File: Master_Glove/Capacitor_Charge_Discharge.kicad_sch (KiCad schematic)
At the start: 22 parts, among them Q1 NPN, Q2 PNP, Q3 NPN, SW1 SW_Push, U2 OPA2340, U3 MIC1553YM5-TR, U4 TC7WH02FU, U5 NC7SZ57P6X, U6 74AHC1G14, U7 TC7WH02FU

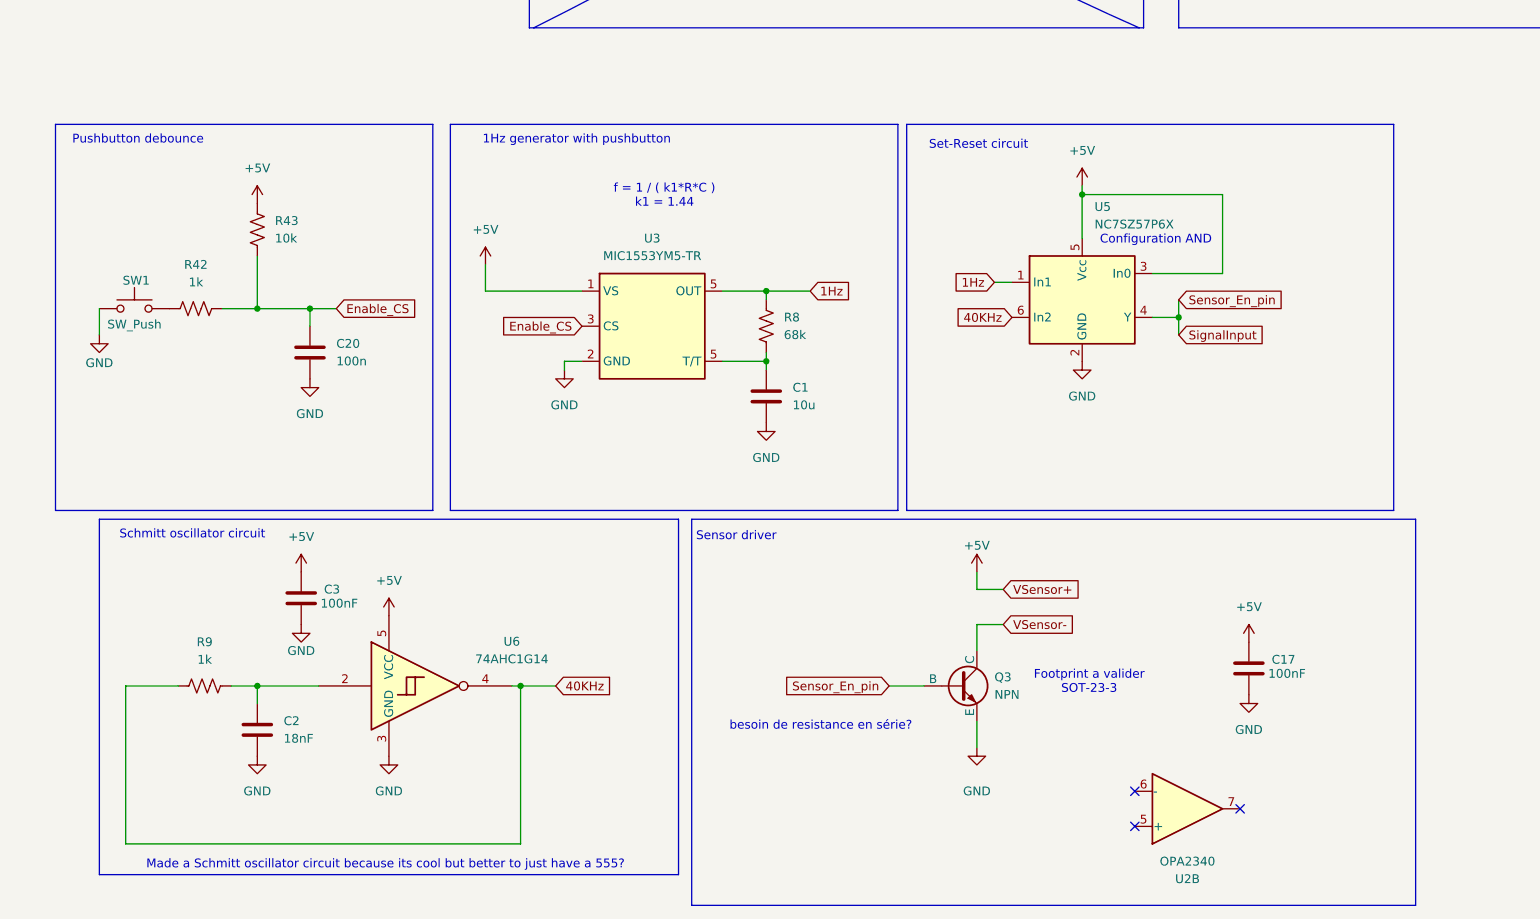
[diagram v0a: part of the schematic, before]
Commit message: fix bug
added comment for resistor in series for sensor not needed since already built in NPN
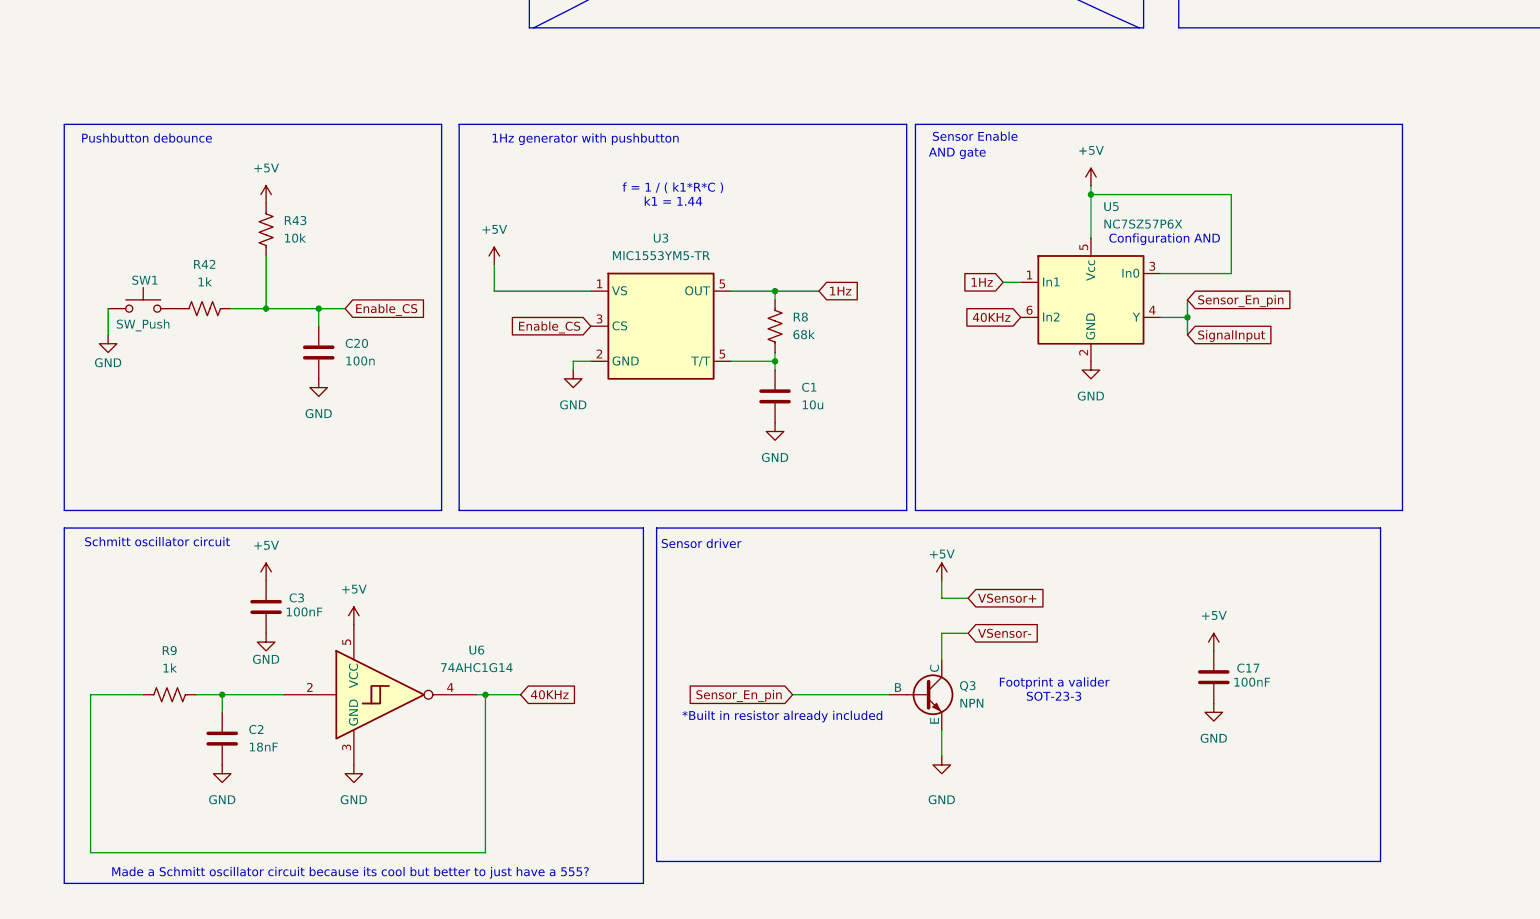
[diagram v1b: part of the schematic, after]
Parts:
- removed U2: OPA2340, symbol Amplifier_Operational:OPA2340
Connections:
- no-connect marks 6 -> 3
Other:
- note added: "*Built in resistor already included"
- note added: "AND gate"
- note added: "Sensor Enable"
- note removed: "Set-Reset circuit"
- note removed: "besoin de resistance en série?"
- moved on the sheet: C1, C17, C2, C20, C3, Q3, R42, R43, R8, R9, SW1, U3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

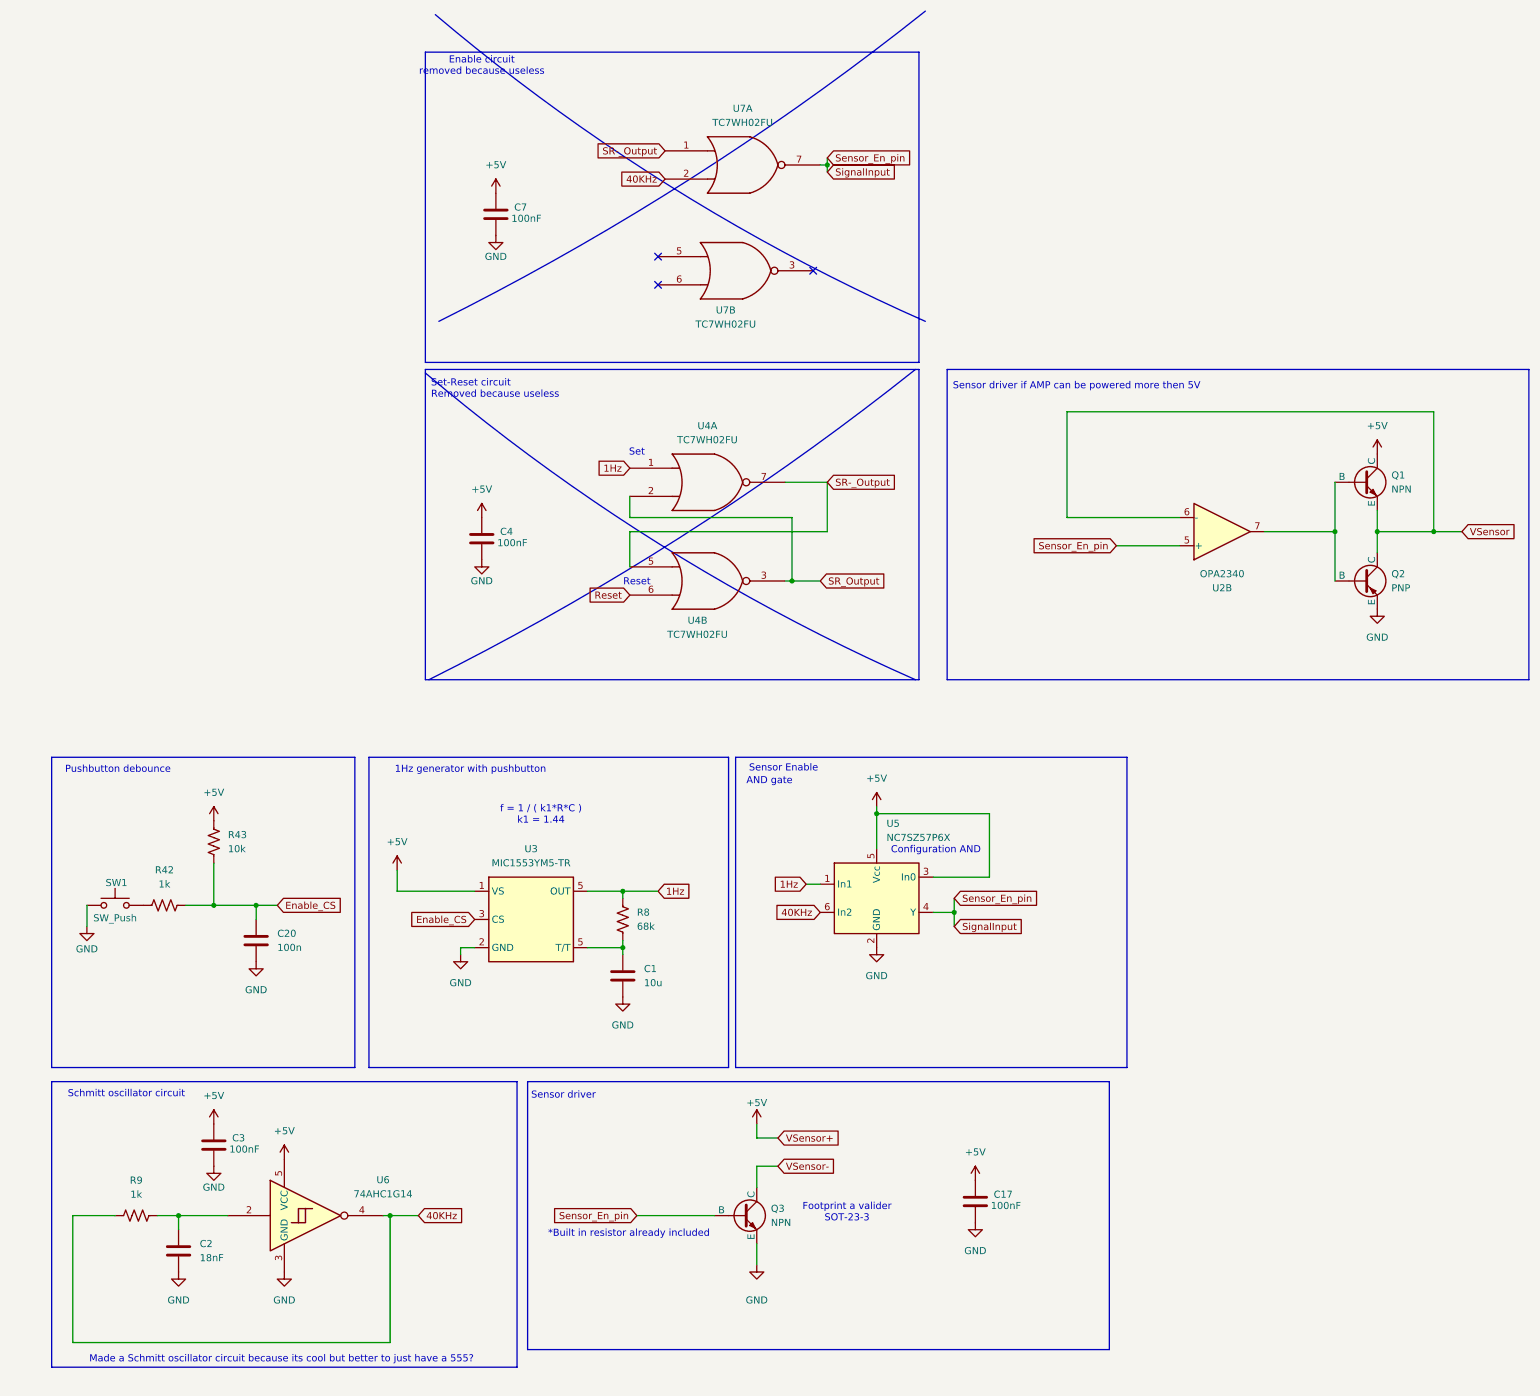
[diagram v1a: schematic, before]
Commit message: Adding footprints
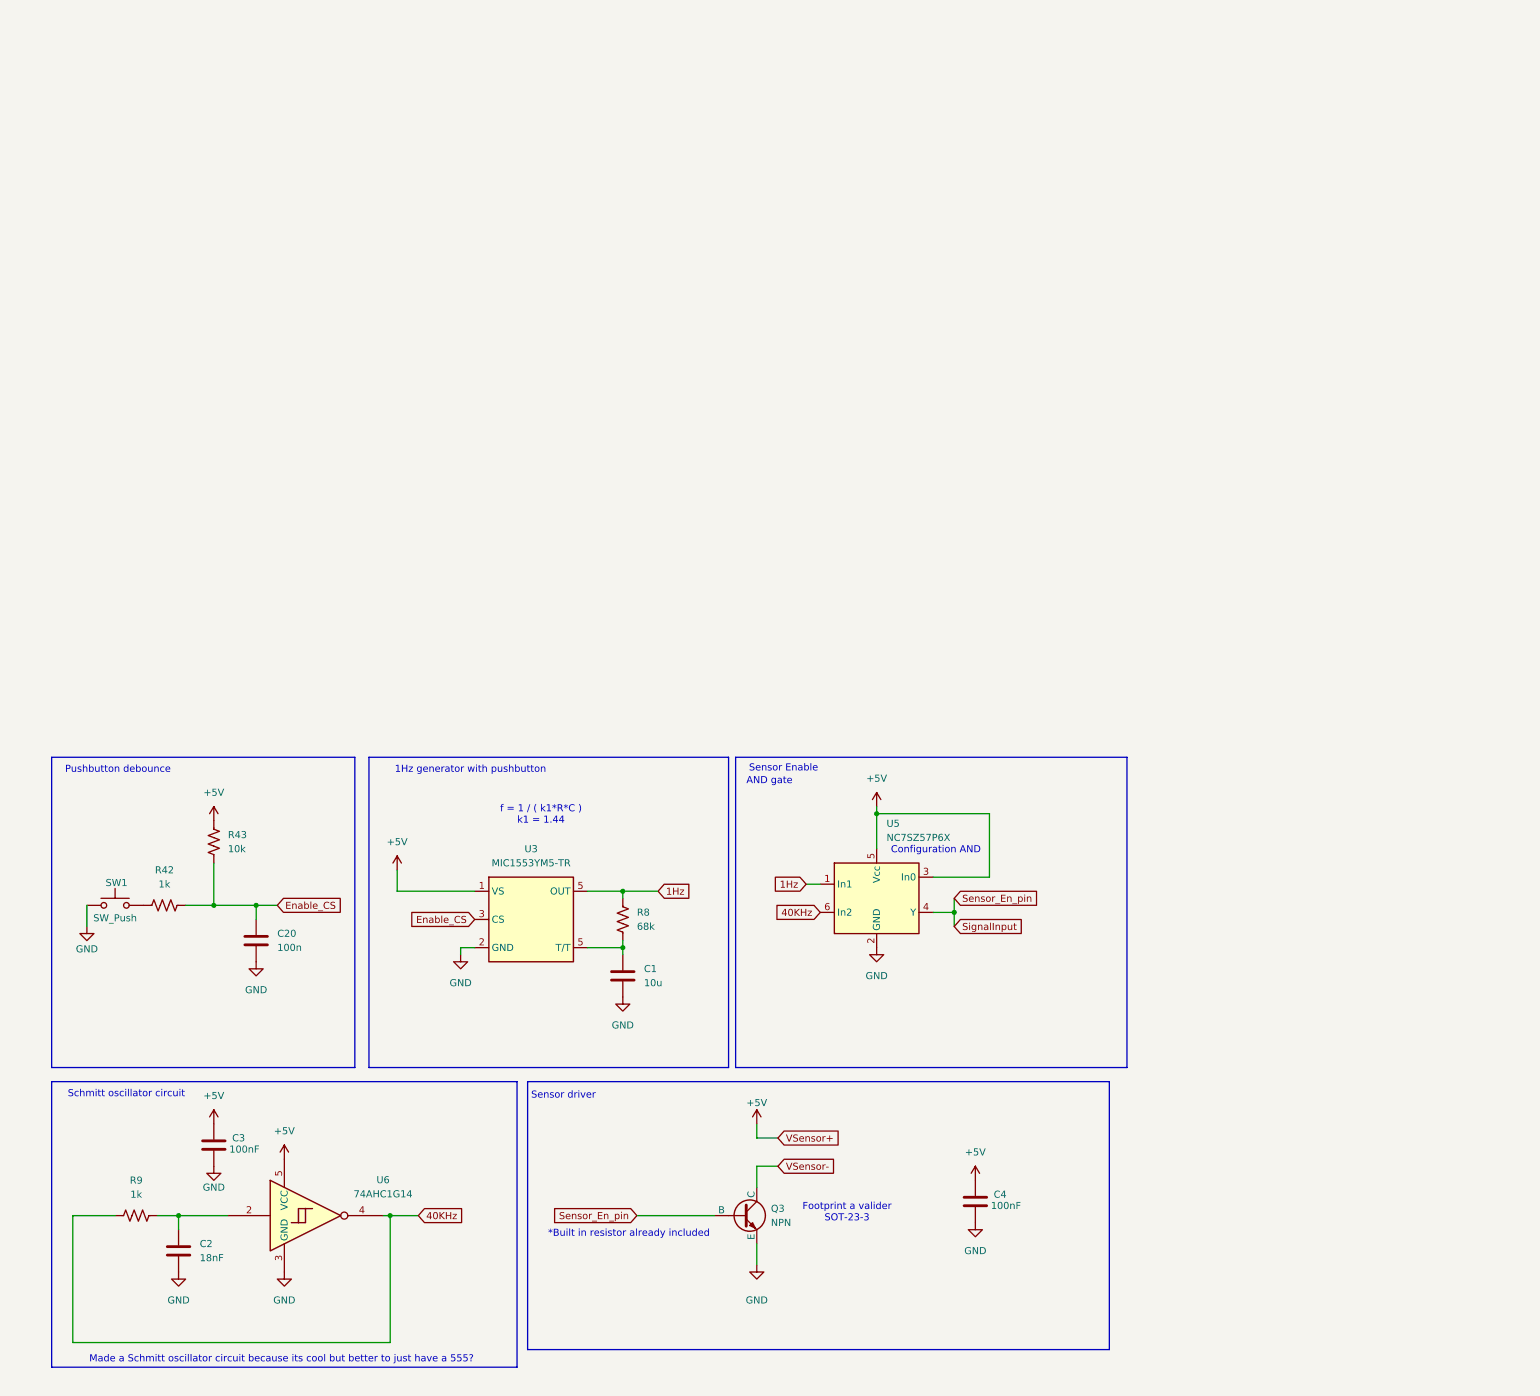
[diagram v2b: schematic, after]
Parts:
- removed C4, C7: 100nF, symbol Device:C
- removed Q1: NPN, symbol Simulation_SPICE:NPN
- removed Q2: PNP, symbol Simulation_SPICE:PNP
- removed U2: OPA2340, symbol Amplifier_Operational:OPA2340
- removed U4, U7: TC7WH02FU, symbol 74xGxx:74AUC2G02
- renumbered C17 to C4
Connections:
- no-connect marks 3 -> 0
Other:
- note removed: "Enable circuit removed because useless"
- note removed: "Reset"
- note removed: "Sensor driver if AMP can be powered more then 5V"
- note removed: "Set"
- note removed: "Set-Reset circuit Removed because useless"

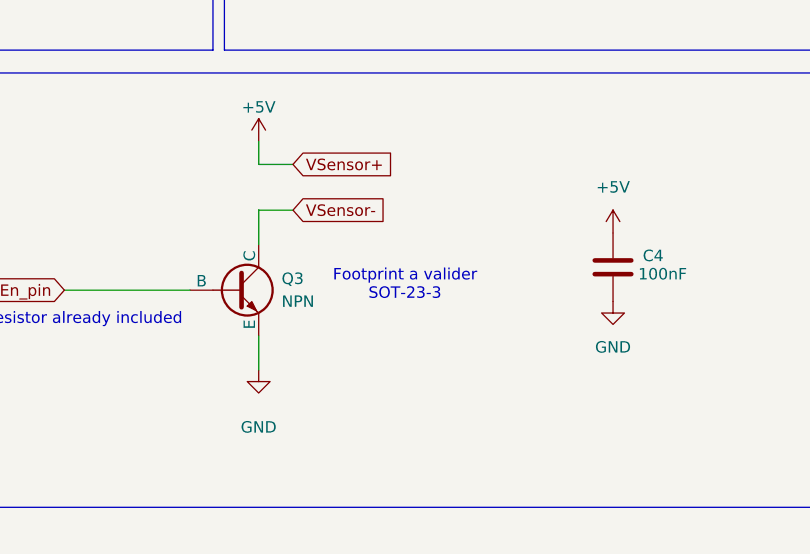
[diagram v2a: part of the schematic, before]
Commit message: added footprints
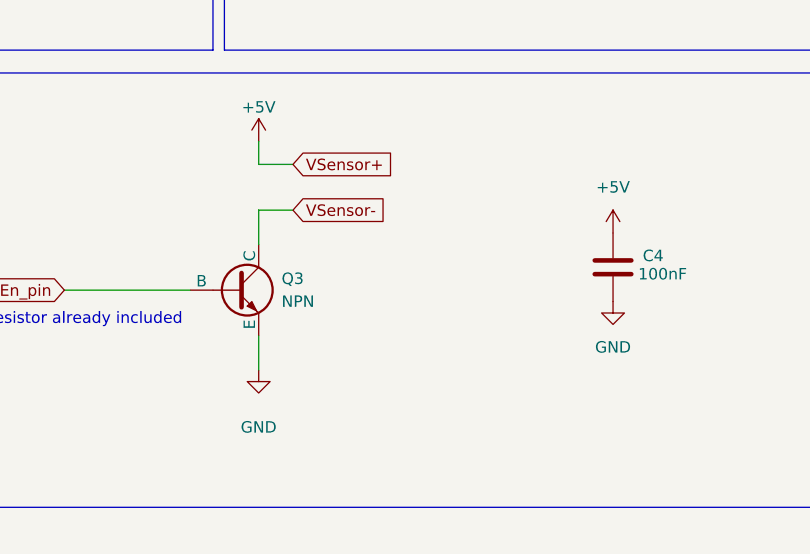
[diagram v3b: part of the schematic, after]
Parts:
- Q3: footprint (none) -> Library:SOT-23 MMUN2211LT1G
- U6: footprint (none) -> Library:SOT-353-1_74LVC1G14GW,125
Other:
- note removed: "Footprint a valider SOT-23-3"
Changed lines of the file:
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@@
-		)
-	)
-	(text "Footprint a valider\nSOT-23-3"
-		(exclude_from_sim no)
-		(at 158.496 101.092 0)
-		(effects
-			(font
-				(size 1.27 1.27)
-			)
 		)
 	)
@@
 			)
 		)
-		(property "Footprint" ""
+		(property "Footprint" "Library:SOT-353-1_74LVC1G14GW,125"
 			(at 62.23 101.6 0)
 			(effects
@@
 			)
 		)
-		(property "Footprint" ""
+		(property "Footprint" "Library:SOT-23 MMUN2211LT1G"
 			(at 203.2 101.6 0)
 			(effects
@@
 			)
 		)
-		(property "Sim.Pins" "1=C 2=B 3=E"
+		(property "Sim.Pins" "1=B 2=E 3=C "
 			(at 139.7 101.6 0)
 			(effects
